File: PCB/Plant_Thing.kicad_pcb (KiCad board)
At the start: 4 copper layers, 37.4 x 59.8 mm, 56 parts, among them IC1 NCP333FCT2G, J1 Conn_ARM_SWD_TagConnect_TC203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, J3 Conn_Coaxial_Small, Q1 NMOS, Q2 NMOS, U1 nRF52820-QDxx, U2 BQ297xy, U3 BQ24090DGQ, U4 LTR-303ALS-01

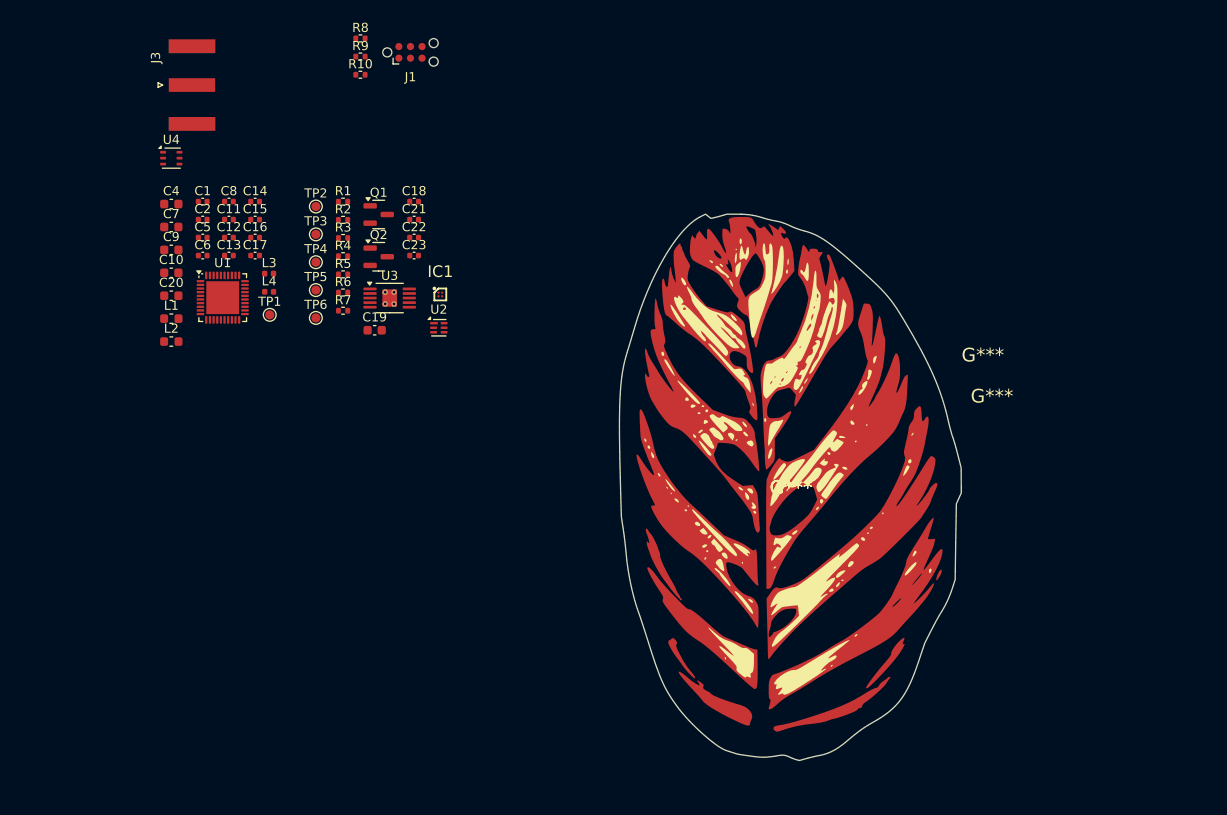
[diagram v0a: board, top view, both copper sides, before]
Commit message: Added LED Driver IC for the led bar inside the calathea leaf
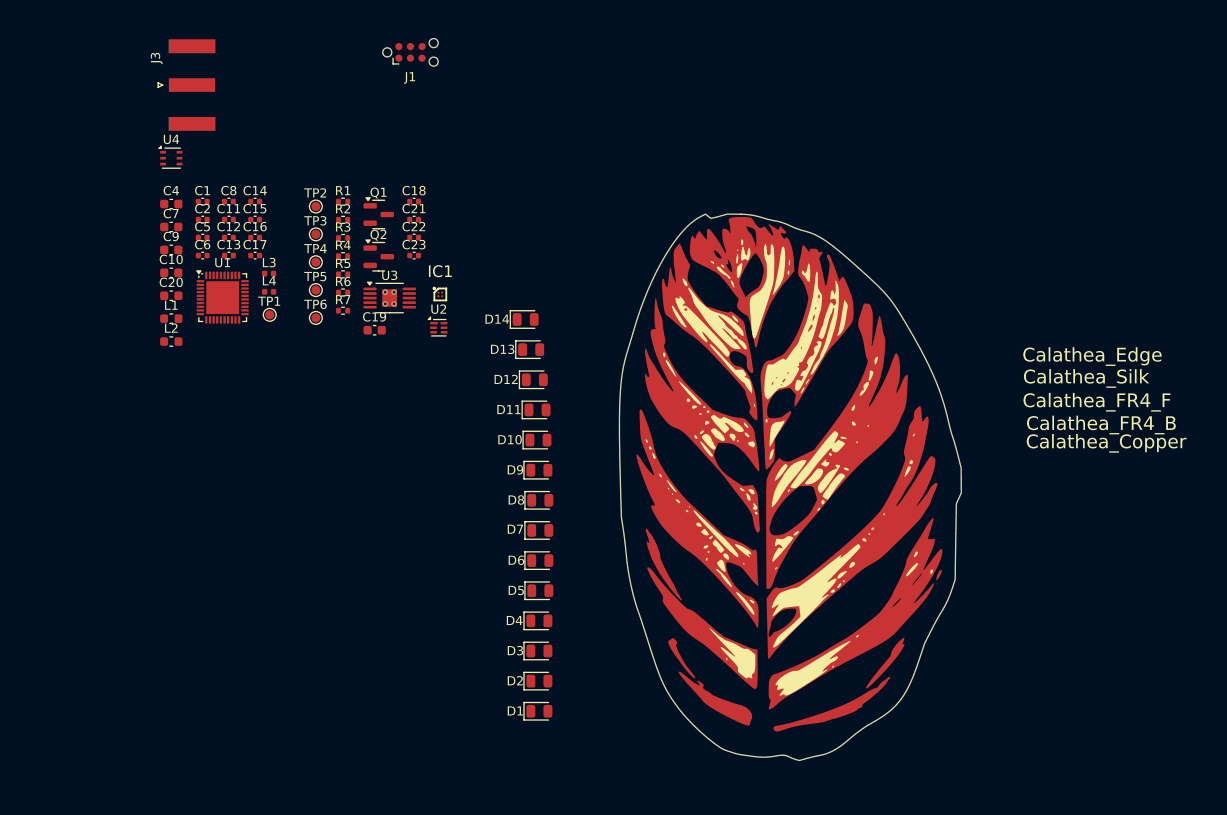
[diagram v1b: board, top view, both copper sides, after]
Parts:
- removed G***: LOGO, calathea:calathea_silk
- removed R10, R8, R9: 330, Resistor_SMD:R_0402_1005Metric
- added Calathea_Silk: LOGO, calathea:calathea_silk, F.Cu at (150.2, 100.1)
- added D1: LED, LED_SMD:LED_0805_2012Metric, F.Cu at (122.4, 124.5)
- added D10: LED, LED_SMD:LED_0805_2012Metric, F.Cu at (122.3, 94.8)
- added D11: LED, LED_SMD:LED_0805_2012Metric, F.Cu at (122.2, 91.5)
- added D12: LED, LED_SMD:LED_0805_2012Metric, F.Cu at (121.9, 88.2)
- added D13: LED, LED_SMD:LED_0805_2012Metric, F.Cu at (121.5, 84.9)
- added D14: LED, LED_SMD:LED_0805_2012Metric, F.Cu at (120.9, 81.6)
- added D2: LED, LED_SMD:LED_0805_2012Metric, F.Cu at (122.4, 121.2)
- added D3: LED, LED_SMD:LED_0805_2012Metric, F.Cu at (122.4, 117.9)
- added D4: LED, LED_SMD:LED_0805_2012Metric, F.Cu at (122.4, 114.6)
- added D5: LED, LED_SMD:LED_0805_2012Metric, F.Cu at (122.5, 111.3)
- added D6: LED, LED_SMD:LED_0805_2012Metric, F.Cu at (122.5, 108.0)
- added D7: LED, LED_SMD:LED_0805_2012Metric, F.Cu at (122.5, 104.7)
- added D8: LED, LED_SMD:LED_0805_2012Metric, F.Cu at (122.5, 101.4)
- added D9: LED, LED_SMD:LED_0805_2012Metric, F.Cu at (122.4, 98.1)
- renumbered G*** to Calathea_Copper, G*** to Calathea_Edge, G*** to Calathea_FR4_B, G*** to Calathea_FR4_F

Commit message: added dcdc for external components. Changed board edge to a rect for easier dev board routuing.
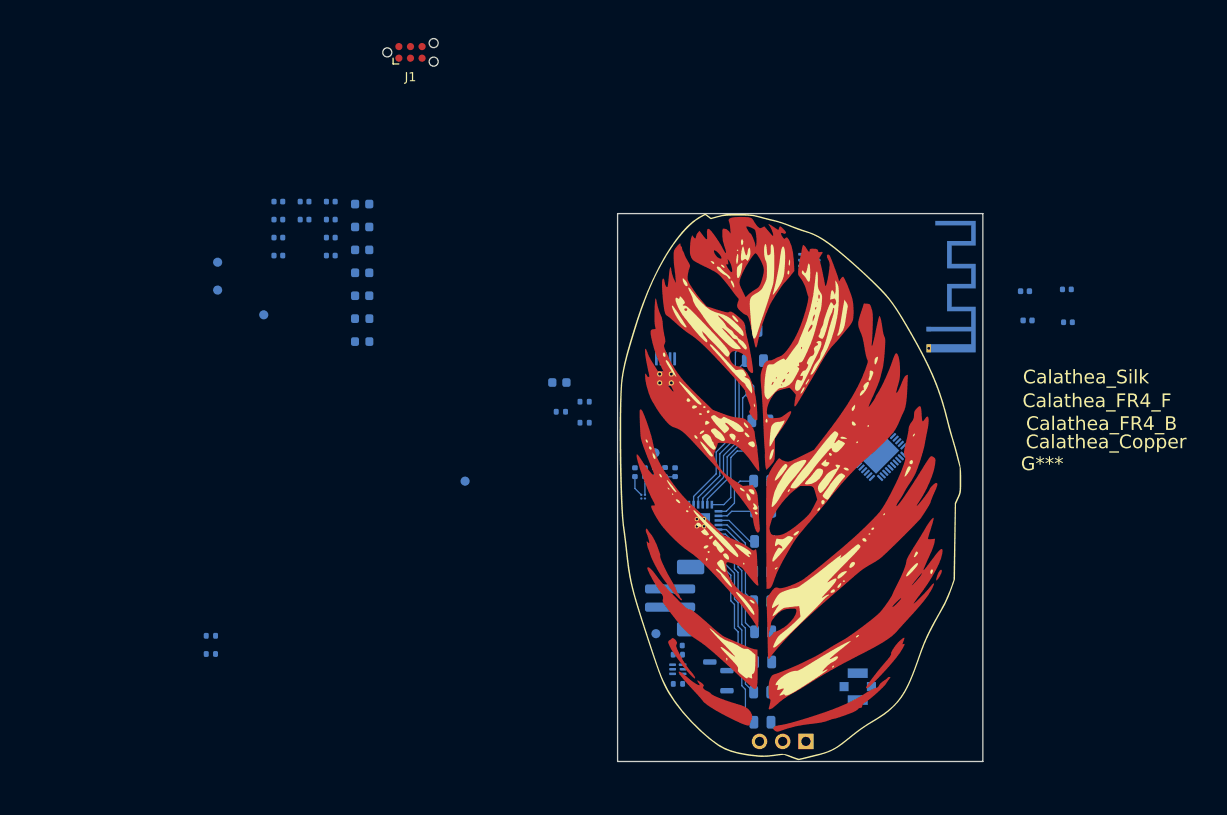
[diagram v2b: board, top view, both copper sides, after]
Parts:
- removed Calathea_Edge: LOGO, calathea:calathea_edge2
- added AE1: Antenna, RF_Antenna:Texas_SWRA117D_2.4GHz_Right, B.Cu at (165.1, 82.7)
- added BT1: Battery_Cell, Connector_JST:JST_PH_B2B-PH-SM4-TB_1x02-1MP_P2.00mm_Vertical, B.Cu at (137.2, 112.1)
- added G***: LOGO, calathea:calathea_edge_silk, F.Cu at (149.9, 100.0)
- added J4: Conn_01x03_Socket, Connector_PinSocket_2.54mm:PinSocket_1x03_P2.54mm_Horizontal, B.Cu at (151.6, 127.8)
- added R8: 2k2, Resistor_SMD:R_0402_1005Metric, B.Cu at (86.5, 116.2)
- added R9: 2k2, Resistor_SMD:R_0402_1005Metric, B.Cu at (86.5, 118.2)
- added U5: TLC59283RGER, TLC59283RGER:RGE24_2P1X2P1_TEX, B.Cu at (140.1, 103.9)
- C1, C10, C11, C12, C13, C14, C15, C16, C17, C18, C19, C2, C20, C21, C22, C23, C4, C5, C6, C7, C8, C9, IC1, L1, L2, L3, L4, Q1, Q2, R1, R2, R3, R4, R5, R6, R7, TP1, TP2, TP3, TP4, TP5, TP6, U1, U2, U3, U4: moved to B.Cu
- D1, D10, D11, D12, D13, D14, D2, D3, D4, D5, D6, D7, D8, D9: value LED -> LED_Small; moved to B.Cu
- J3: footprint Connector_Coaxial:SMA_Amphenol_132289_EdgeMount -> Connector_Coaxial:U.FL_Molex_MCRF_73412-0110_Vertical; moved to B.Cu
- moved J3 98.3 mm to (157.3, 121.8), turned to 90 degrees
- moved C13 92.2 mm to (180.3, 81.9), turned to 180 degrees
- moved C12 91.9 mm to (180.2, 78.3), turned to 180 degrees
- moved L4 83.1 mm to (175.9, 81.7), turned to 180 degrees
- moved L3 82.8 mm to (175.6, 78.5), turned to 180 degrees
- moved U1 73.5 mm to (159.3, 96.0), turned to 45 degrees
- moved U4 70.8 mm to (152.0, 75.1), turned to 180 degrees
- moved Q1 64.8 mm to (142.0, 123.2), turned to 180 degrees
- moved R1 64.3 mm to (137.6, 121.5)
- moved R2 60.1 mm to (137.6, 118.3), turned to 180 degrees
- moved Q2 57.9 mm to (142.0, 119.1), turned to 180 degrees
- moved C18 56.5 mm to (137.6, 117.3)
- moved D14 51.2 mm to (146.9, 125.7)
- moved TP6 50.8 mm to (135.2, 116.0), turned to 180 degrees
- moved D1 47.6 mm to (145.4, 82.8)
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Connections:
- D1 pad 1: unconnected-(D1-K-Pad1) -> Net-(D1-K)
- D10 pad 1: unconnected-(D10-K-Pad1) -> Net-(D10-K)
- D11 pad 1: unconnected-(D11-K-Pad1) -> Net-(D11-K)
- D12 pad 1: unconnected-(D12-K-Pad1) -> Net-(D12-K)
- D13 pad 1: unconnected-(D13-K-Pad1) -> Net-(D13-K)
- D14 pad 1: unconnected-(D14-K-Pad1) -> Net-(D14-K)
- D2 pad 1: unconnected-(D2-K-Pad1) -> Net-(D2-K)
- D3 pad 1: unconnected-(D3-K-Pad1) -> Net-(D3-K)
- D4 pad 1: unconnected-(D4-K-Pad1) -> Net-(D4-K)
- D5 pad 1: unconnected-(D5-K-Pad1) -> Net-(D5-K)
- D6 pad 1: unconnected-(D6-K-Pad1) -> Net-(D6-K)
- D7 pad 1: unconnected-(D7-K-Pad1) -> Net-(D7-K)
- D8 pad 1: unconnected-(D8-K-Pad1) -> Net-(D8-K)
- D9 pad 1: unconnected-(D9-K-Pad1) -> Net-(D9-K)
- L4 pad 1: unconnected-(L4-Pad1) -> Net-(AE1-A)
- U1 pad 17: unconnected-(U1-P0.20-Pad17) -> P0.20_BLANK
- U1 pad 32: P0.29_LED_G -> P0.29_SCLK
- U1 pad 33: P0.30_LED_B -> P0.30_SIN
- U1 pad 34: P0.28_LED_R -> P0.28_LAT
- U1 pad 35: unconnected-(U1-AIN1/P0.03-Pad35) -> P0.03_TDT_MEASURE
- U4 pad 1: unconnected-(U4-VDD-Pad1) -> VDDA
- U4 pad 3: unconnected-(U4-GND-Pad3) -> GND
- U4 pad 4: unconnected-(U4-SCL-Pad4) -> P0.14_SCL
- U4 pad 6: unconnected-(U4-SDA-Pad6) -> P0.15_SDA
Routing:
- net Net-(D14-K): track 0.00 -> 22.2 mm
- net Net-(D1-K): track 0.00 -> 21.2 mm
- net Net-(D13-K): track 0.00 -> 18.7 mm
- net Net-(D2-K): track 0.00 -> 18.0 mm
- net Net-(D12-K): track 0.00 -> 15.4 mm
- net Net-(D3-K): track 0.00 -> 14.6 mm
- net Net-(D11-K): track 0.00 -> 12.8 mm
- net Net-(D4-K): track 0.00 -> 11.2 mm
- net Net-(D10-K): track 0.00 -> 9.99 mm
- net Net-(D5-K): track 0.00 -> 9.49 mm
- net Net-(D9-K): track 0.00 -> 7.25 mm
- net Net-(D6-K): track 0.00 -> 6.27 mm
- net Net-(D8-K): track 0.00 -> 4.90 mm
- net P0.02_BATT_MEASURE: track 0.00 -> 4.25 mm
- net Net-(D7-K): track 0.00 -> 4.16 mm
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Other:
- board size 37.4 x 59.8 mm -> 40 x 60 mm

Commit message: redid the pcb layout for a more bigger devboard approach. Added a few more components and the antenna.
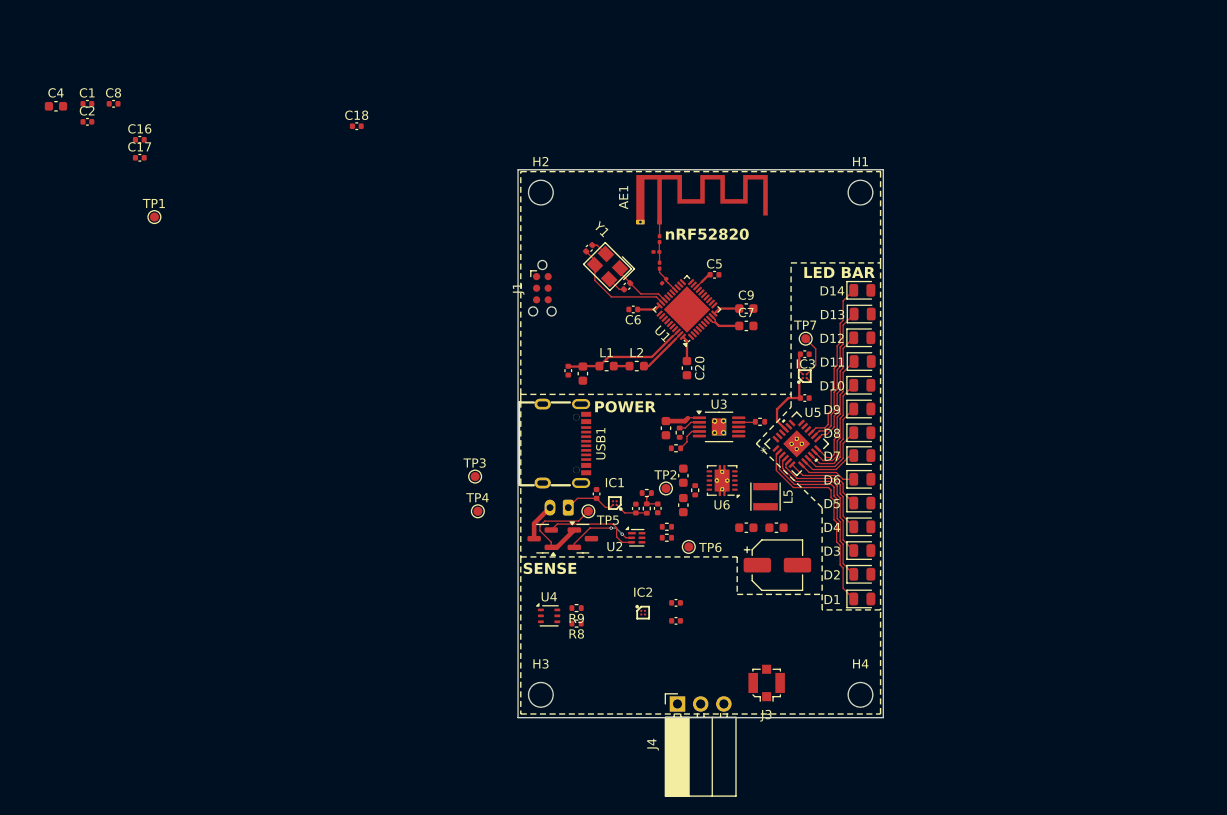
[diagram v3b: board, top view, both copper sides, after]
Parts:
- removed Calathea_Copper: Copper, calathea:calathea_copper
- removed Calathea_FR4_B: LOGO, calathea:calathea_fr4_back
- removed Calathea_FR4_F: FR4, calathea:calathea_fr4
- removed Calathea_Silk: LOGO, calathea:calathea_silk
- removed G***: LOGO, calathea:calathea_edge_silk
- added C24: 10u, Capacitor_SMD:C_0603_1608Metric, F.Cu at (138.2, 98.7)
- added C25: 100n, Capacitor_SMD:C_0603_1608Metric, F.Cu at (138.2, 101.9)
- added C26: 10u, Capacitor_SMD:C_0603_1608Metric, F.Cu at (145.1, 104.4)
- added C27: 10u, Capacitor_SMD:C_0603_1608Metric, F.Cu at (148.4, 104.4)
- added C28: 10u, Capacitor_SMD:CP_Elec_5x4.4, F.Cu at (148.5, 108.5)
- added C29: 1u, Capacitor_SMD:C_0402_1005Metric, F.Cu at (137.4, 112.6)
- added C30: 100n, Capacitor_SMD:C_0402_1005Metric, F.Cu at (137.4, 114.6)
- added C31: 100n, Capacitor_SMD:C_0402_1005Metric, F.Cu at (151.5, 85.4)
- added C32: 100n, Capacitor_SMD:C_0402_1005Metric, F.Cu at (151.5, 90.2)
- added H1: MountingHole, MountingHole:MountingHole_2.7mm_M2.5_DIN965, F.Cu at (157.6, 67.7)
- added H2: MountingHole, MountingHole:MountingHole_2.7mm_M2.5_DIN965, F.Cu at (122.6, 67.7)
- added H3: MountingHole, MountingHole:MountingHole_2.7mm_M2.5_DIN965, F.Cu at (122.6, 122.7)
- added H4: MountingHole, MountingHole:MountingHole_2.7mm_M2.5_DIN965, F.Cu at (157.6, 122.7)
- added IC2: NCP333FCT2G, NCP333FCT2G:BGA4C40P2X2_76X76X63, F.Cu at (133.8, 113.7)
- added IC3: NCP333FCT2G, NCP333FCT2G:BGA4C40P2X2_76X76X63, F.Cu at (151.5, 87.8)
- added L5: NR3015T2R2M, Inductor_SMD:L_Taiyo-Yuden_NR-30xx, F.Cu at (147.2, 101.0)
- added R10: 100, Resistor_SMD:R_0402_1005Metric, F.Cu at (139.5, 100.3)
- added TP7: TestPoint_Small, TestPoint:TestPoint_Pad_D1.0mm, F.Cu at (151.6, 83.7)
- added U6: TPS63001, Package_SON:Texas_DRC0010J_ThermalVias, F.Cu at (142.4, 99.2)
- added USB1: TYPE-C 16PIN 2MD(073), USB-C-SMD_TYPE-C-6PIN-2MD-073:USB-C-SMD_TYPE-C-6PIN-2MD-073, F.Cu at (125.2, 95.2)
- added Y1: 32M, X322532MOB4SI:CRYSTAL-SMD_4P-L3.2-W2.5-BL, F.Cu at (129.9, 75.8)
- AE1, C1, C10, C11, C14, C15, C16, C17, C18, C19, C2, C20, C21, C22, C23, C4, C5, C6, C7, C8, C9, D1, D10, D11, D12, D13, D14, D2, D3, D4, D5, D6, D7, D8, D9, IC1, J3, J4, L1, L2, Q1, Q2, R1, R2, R3, R4, R5, R6, R7, R8, R9, TP1, TP2, TP3, TP4, TP5, TP6, U1, U2, U3, U4, U5: moved to F.Cu
- BT1: footprint Connector_JST:JST_PH_B2B-PH-SM4-TB_1x02-1MP_P2.00mm_Vertical -> Connector_JST:JST_PH_S2B-PH-K_1x02_P2.00mm_Horizontal
- C12, C13: footprint Capacitor_SMD:C_0402_1005Metric -> Capacitor_SMD:C_0201_0603Metric; moved to F.Cu
- L3, L4: footprint Inductor_SMD:L_0402_1005Metric -> Inductor_SMD:L_0201_0603Metric; moved to F.Cu
- moved C18 66.9 mm to (102.4, 60.4)
- moved D14 48.5 mm to (157.8, 78.4)
- moved U4 48.3 mm to (123.5, 114.0), turned to 0 degrees
- moved TP5 47.3 mm to (127.8, 102.6), turned to 0 degrees
- moved C13 45.7 mm to (135.3, 74.2)
- moved C12 44.1 mm to (136.1, 77.4), turned to -135 degrees
- moved C7 43.4 mm to (145.1, 82.3), turned to 0 degrees
- moved D13 42.8 mm to (157.8, 81.0)
- moved C9 42.6 mm to (145.1, 80.4), turned to 0 degrees
- moved C5 42.2 mm to (141.6, 76.7), turned to 0 degrees
- moved L4 41.3 mm to (135.6, 72.8), turned to -90 degrees
- moved R9 40.4 mm to (126.5, 113.2)
- moved L3 40.1 mm to (135.6, 75.7), turned to -90 degrees
- moved R8 40.1 mm to (126.5, 114.9)
- moved TP4 39.4 mm to (115.7, 102.6), turned to 0 degrees
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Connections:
- U1 pad 31: unconnected-(U1-P0.08-Pad31) -> P0.08_EN_LED
- U5 pad 21: unconnected-(U5-VCC-Pad21) -> Net-(IC3-OUT)
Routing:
- net DEC4: track 0.00 -> 13.6 mm
- net Net-(Q1-D): track 0.00 -> 12.1 mm
- net Net-(U1-XC2): track 0.00 -> 12.0 mm
- net VDD: track 0.00 -> 11.9 mm
- net Net-(Q2-G): track 0.00 -> 10.5 mm
- net Net-(IC3-OUT): track 0.00 -> 8.08 mm
- net Net-(Q1-G): track 0.00 -> 7.81 mm, vias 0 -> 2
- net VBUS: track 0.00 -> 6.72 mm
- net Net-(U1-XC1): track 0.00 -> 6.65 mm
- net DCC: track 0.00 -> 5.43 mm
- net P0.08_EN_LED: track 0.00 -> 4.77 mm
- net GND: track 0.00 -> 4.53 mm
- net -BATT: track 0.00 -> 4.22 mm
- net Net-(D14-K): track 22.2 -> 18.1 mm
- net +BATT: track 2.29 -> 5.86 mm
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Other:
- copper layers 4 -> 2
- board text added: "LED BAR"
- board text added: "POWER"
- board text added: "SENSE"
- board text added: "nRF52820"
